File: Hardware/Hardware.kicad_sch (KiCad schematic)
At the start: 46 parts, among them J1 Conn_01x04_Pin, J2 RJ45_LED_Shielded, J3 USB_A, SW1 SW_SPST, SW2 SW_Push, SW3 SW_Push, SW4 SW_Push, SW5 SW_Push, SW6 SW_Push, SW7 SW_Push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

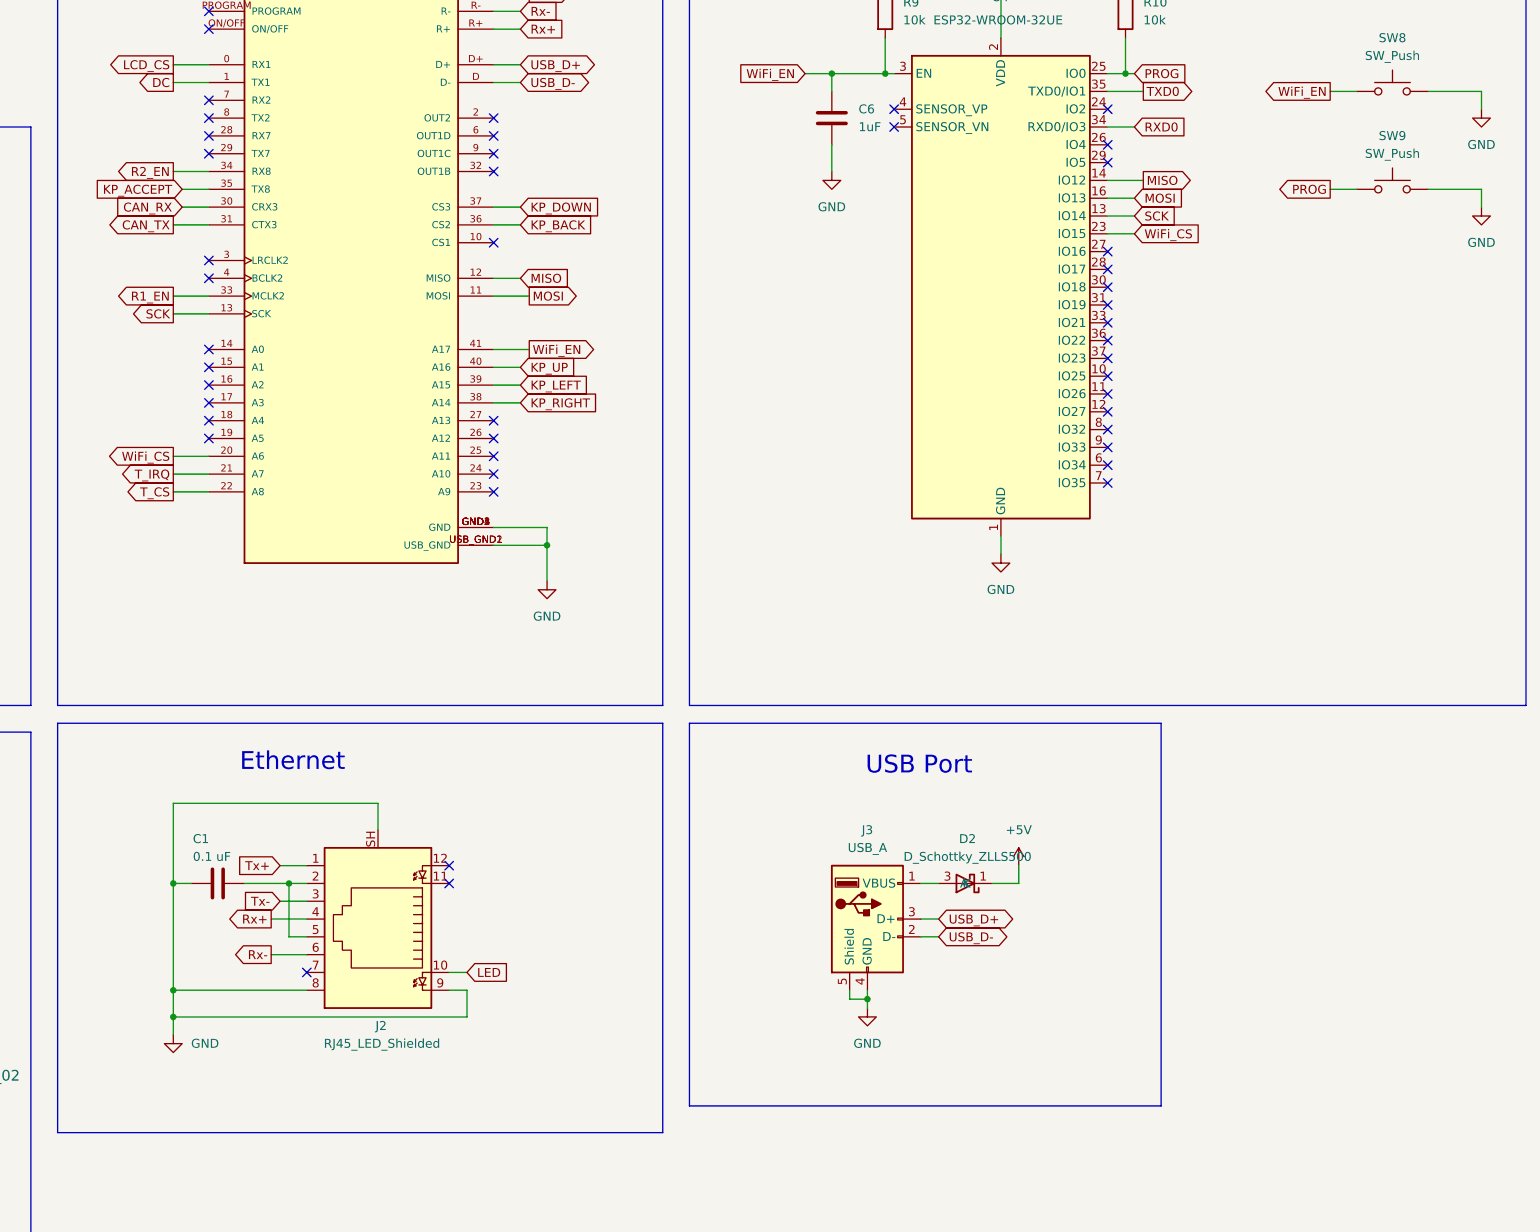
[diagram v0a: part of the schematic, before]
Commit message: fixed silkscreens and added servo tester
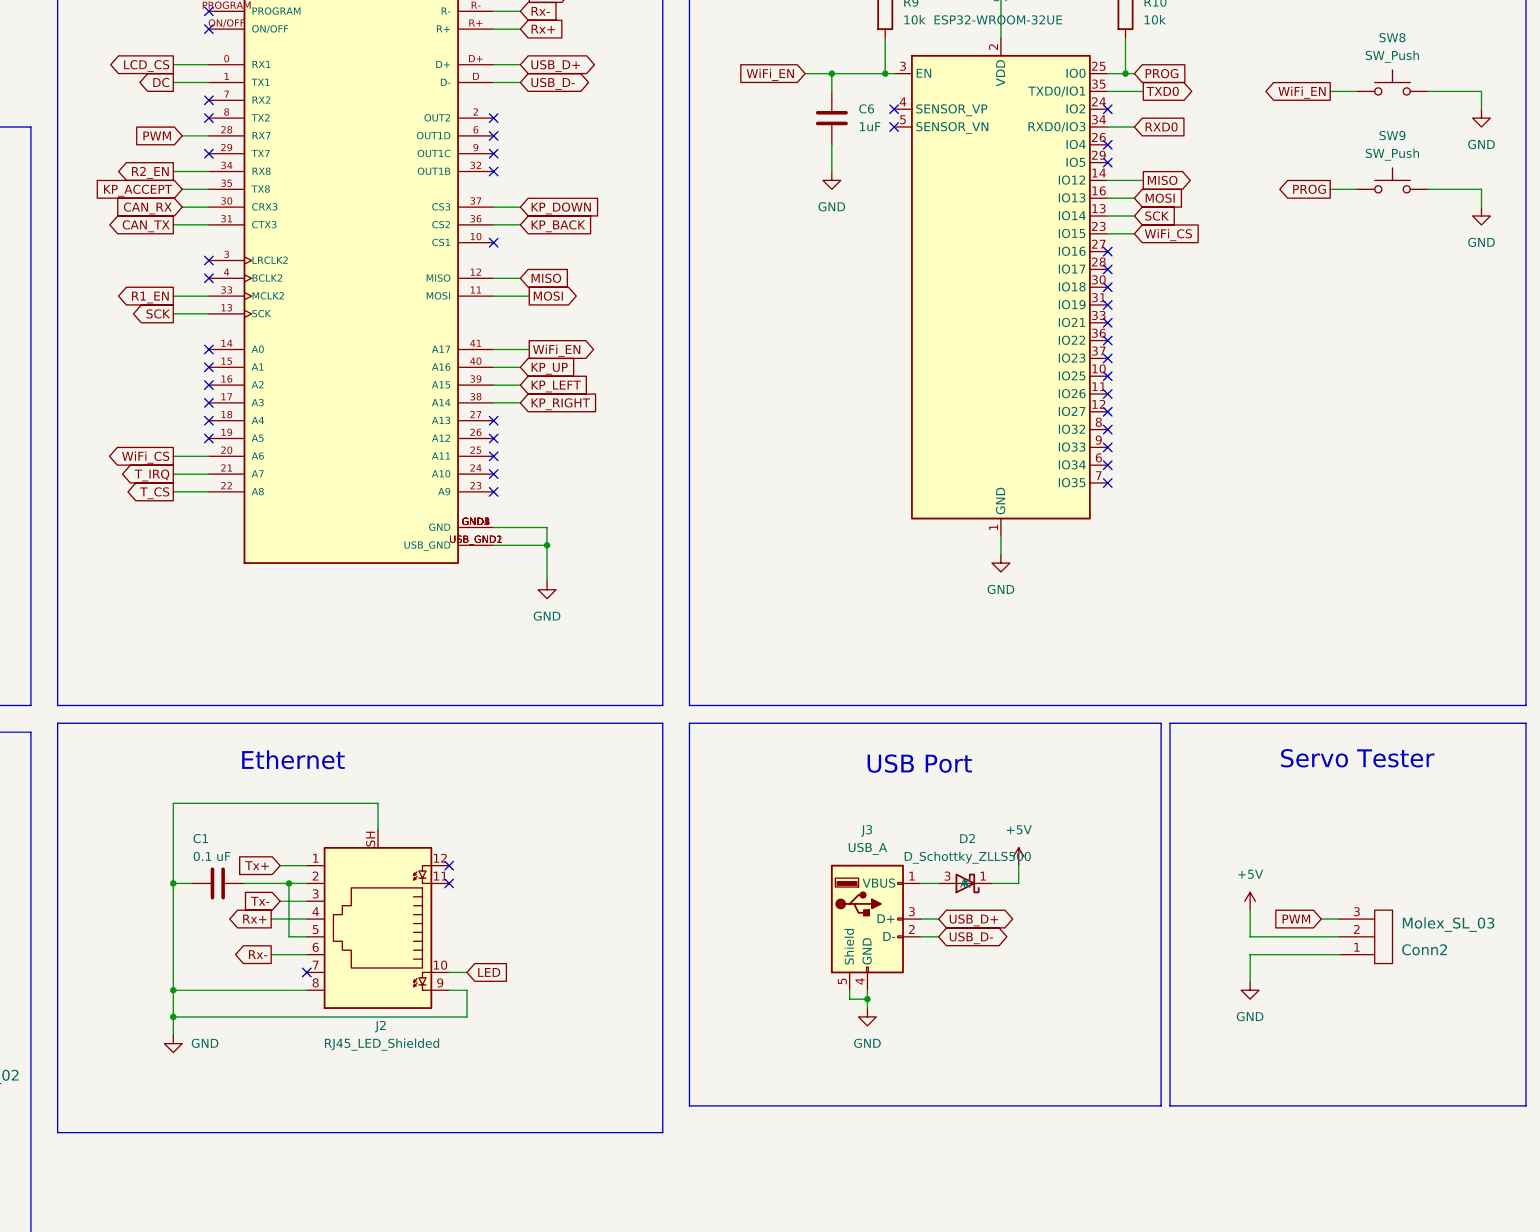
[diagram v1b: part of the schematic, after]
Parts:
- added Conn2: Molex_SL_03, Connector_JST:JST_PH_B3B-PH-K_1x03_P2.00mm_Vertical, symbol MRDT_Connectors:Molex_SL_03
- Conn1: footprint MRDT_Connectors:MOLEX_SL_02_Horizontal -> Connector_JST:JST_PH_B2B-PH-K_1x02_P2.00mm_Vertical
- D3: footprint LED_SMD:LED_0603_1608Metric_Pad1.05x0.95mm_HandSolder -> LED_THT:LED_D5.0mm
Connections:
- net +5V: now also Conn2.2
- net GND: now also Conn2.1
- net PWM: now reaches U3.28 (RX7)
- net PWM: now also Conn2.3
- no-connect marks 50 -> 49
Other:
- note added: "Servo Tester"
